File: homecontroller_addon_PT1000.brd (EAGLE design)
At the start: 60 x 100 mm, 44 parts, among them U1 OPA2188AIDGKR, U2 OPA2188AIDGKR, U3 REF3025AIDBZTG4, U4 ADS1015IDGST, X1 S2L3.50/10/90G

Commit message: update routing
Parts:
- added C10: 1000pF, supply2:CAPC3216X88N
- added R26: 0 Ohms, Vishay_By_element14_Batch_1:RESC3216X71N
- moved C2 43.4 mm to (31.9, 52.1), turned to 0 degrees
- moved U3 38.8 mm to (31.9, 55.9), turned to 180 degrees
- moved C7 34.5 mm to (3.95, 90.2), turned to 90 degrees
- moved C3 34.5 mm to (31.9, 59.7), turned to 0 degrees
- moved U4 24.8 mm to (8.35, 78.8), turned to 90 degrees
- moved R8 23.2 mm to (29.1, 77.0)
- moved R21 22.9 mm to (28.9, 92.8)
- moved R15 22.9 mm to (28.9, 85.1)
- moved R3 22.5 mm to (28.8, 65.0)
- moved R5 18.0 mm to (29.0, 68.9), turned to 180 degrees
- moved R11 17.6 mm to (29.0, 73.0), turned to 180 degrees
- moved R18 17.5 mm to (29.0, 81.1), turned to 180 degrees
- moved R24 17.5 mm to (29.0, 89.0), turned to 180 degrees
- moved R14 16.7 mm to (22.9, 82.9)
- moved R20 16.6 mm to (22.9, 90.9)
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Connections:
- net N$5 renamed -IN_0
- removed net +IN_1: R12.2, U1.5
- removed net +IN_2: R19.2, U2.3
- removed net +IN_3: R25.2, U2.5
- removed net N$1: R6.2, U1.3
- new net PE: C10.1, RV1.1, RV2.1, RV3.1, RV4.1
- new net SGND: C1.1, C4.1, C8.1, C9.1, R26.2
- net AGND: now also C10.2, R26.1, X1.2, X1.4, X1.6, X1.8; no longer C1.1, C4.1, C8.1, C9.1, RV1.1, RV2.1, RV3.1, RV4.1, X1.1, X1.3, X1.5, X1.7
- net PT1000_0: now also R6.2, U1.3, X1.1; no longer X1.2
- net PT1000_1: now also R12.2, U1.5, X1.3; no longer X1.4
- net PT1000_2: now also R19.2, U2.3, X1.5; no longer X1.6
- net PT1000_3: now also R25.2, U2.5, X1.7; no longer X1.8
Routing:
- net PT1000_3: track 0.00 -> 65.3 mm, vias 0 -> 3
- net PT1000_2: track 0.00 -> 60.4 mm, vias 0 -> 2
- net REF2.0V: track 0.00 -> 55.3 mm, vias 0 -> 5
- net -IN_3: track 0.00 -> 35.5 mm, vias 0 -> 4
- net PT1000_0: track 0.00 -> 31.1 mm, vias 0 -> 1
- net PT1000_1: track 0.00 -> 26.7 mm, vias 0 -> 1
- net AIN3: track 0.00 -> 17.4 mm, vias 0 -> 2
- net AIN2: track 0.00 -> 12.8 mm, vias 0 -> 2
- net -IN_2: track 0.00 -> 8.50 mm, vias 0 -> 2
- net AGND: track 0.00 -> 7.85 mm
- net N$4: track 0.00 -> 5.23 mm
- net VDD5V_F: track 0.00 -> 2.99 mm
- net N$1: track 0.00 -> 1.24 mm
- net N$7: track 0.00 -> 0.74 mm
- added copper zone on layer 1, net SGND
- added copper zone on layer 2, net SGND

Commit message: adopted wire plan
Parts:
- moved U4 2.54 mm to (10.9, 79.0), turned to 180 degrees
- moved U1 0.73 mm to (8.88, 71.1)
- moved R6 0.27 mm to (16.6, 66.9), turned to 180 degrees
- moved R12 0.23 mm to (16.5, 74.9), turned to 180 degrees
- moved R24 0.22 mm to (28.8, 88.9)
- moved R25 0.20 mm to (16.3, 91.0)
- moved R15 0.20 mm to (28.8, 85.1)
- moved R18 0.10 mm to (28.9, 81.1)
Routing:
- net -IN_1: track 0.00 -> 35.5 mm, vias 0 -> 4
- net -IN_2: track 8.50 -> 37.7 mm, vias 2 -> 4
- net PT1000_1: track 26.7 -> 10.2 mm, vias 1 -> 0
- net PT1000_2: track 60.4 -> 67.3 mm
- net AIN2: track 12.8 -> 19.2 mm
- net AGND: track 7.85 -> 14.0 mm, vias 0 -> 4
- net N$3: track 0.00 -> 4.94 mm
- net N$2: track 0.00 -> 4.58 mm
- net VDD5V_F: track 2.99 -> 6.45 mm
- net PT1000_3: track 65.3 -> 68.1 mm, vias 3 -> 2

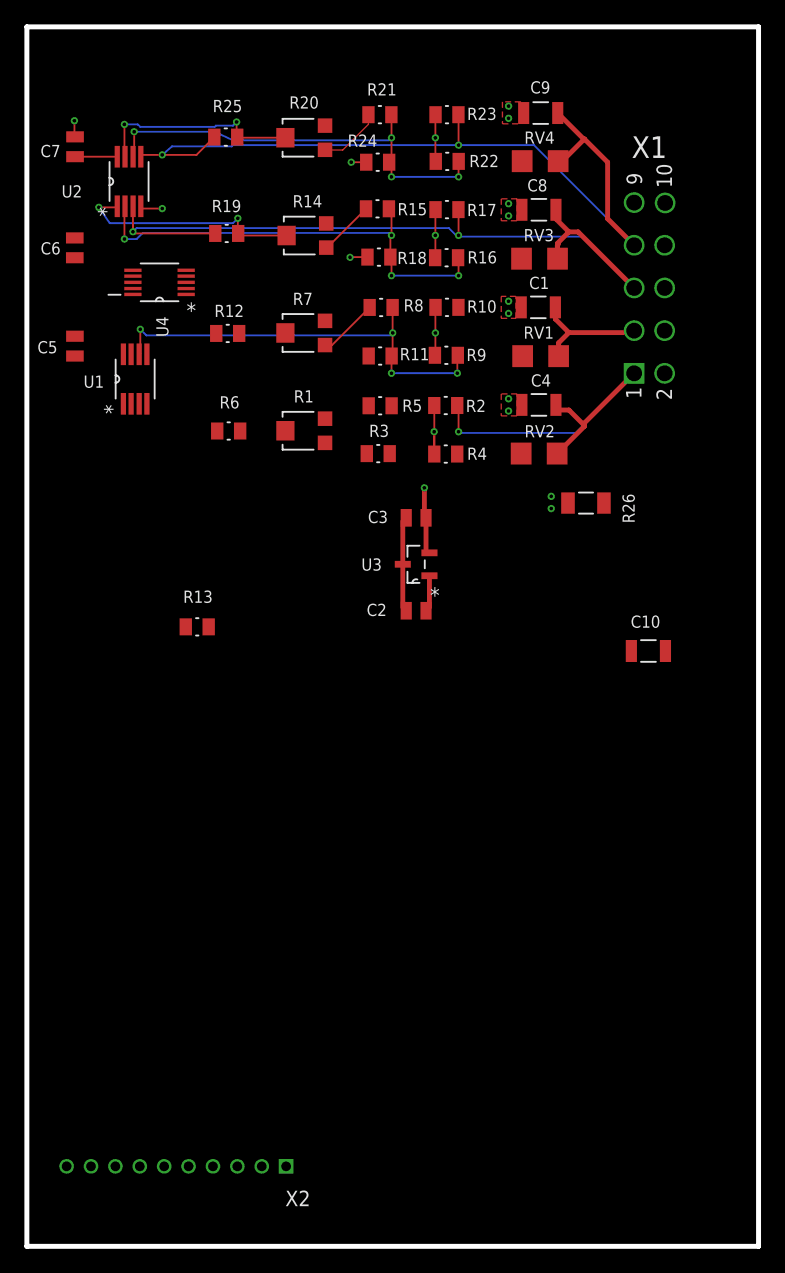
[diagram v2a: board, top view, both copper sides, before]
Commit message: change position of I2C ADC
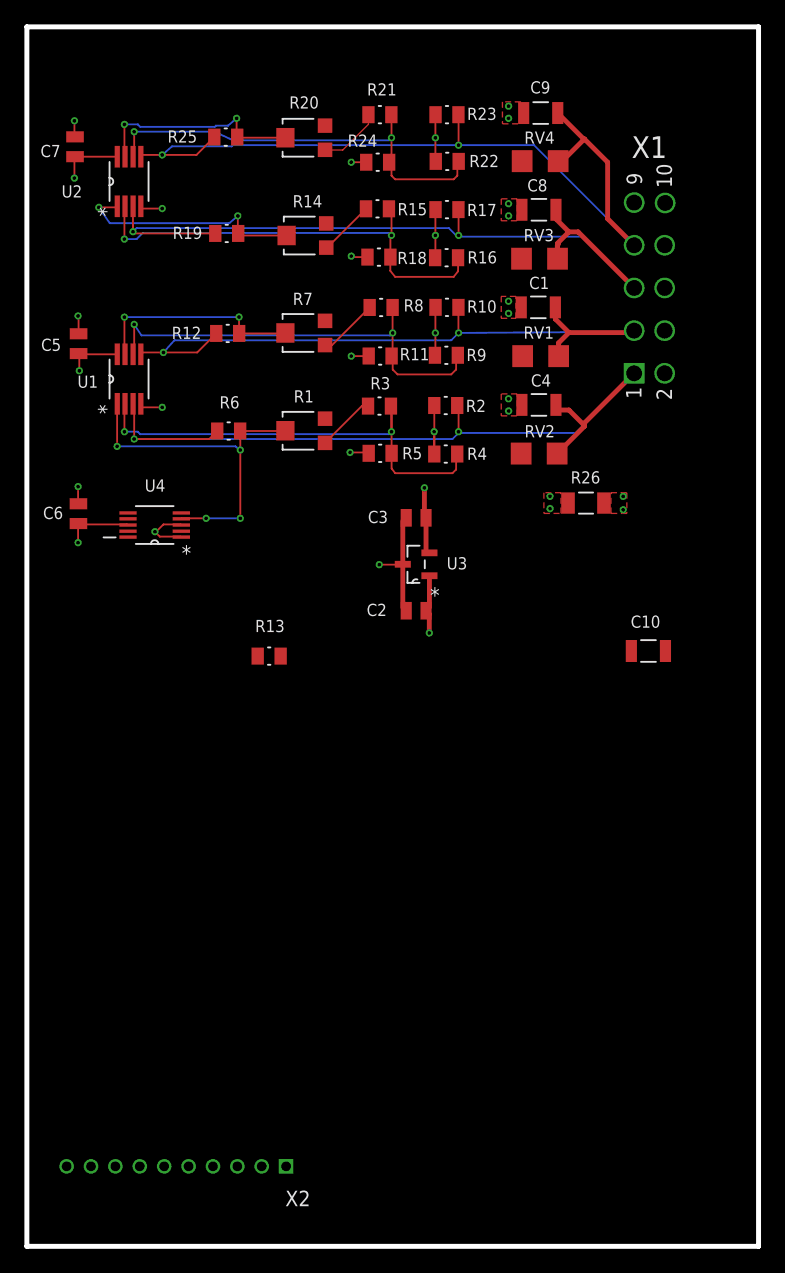
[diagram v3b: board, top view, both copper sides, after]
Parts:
- moved C6 21.8 mm to (4.23, 60.1)
- moved U4 19.9 mm to (10.5, 59.1)
- moved R13 6.37 mm to (19.9, 48.4)
- moved R3 3.90 mm to (28.9, 68.9)
- moved R5 3.90 mm to (29.0, 65.0)
- moved U1 0.50 mm to (8.38, 71.1)
- moved C5 0.36 mm to (4.24, 74.0)
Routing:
- net VDD5V_F: track 6.45 -> 145.6 mm, vias 0 -> 4
- net PT1000_1: track 10.2 -> 58.5 mm, vias 0 -> 2
- net -IN_0: track 0.00 -> 38.5 mm, vias 0 -> 2
- net PT1000_0: track 31.1 -> 68.2 mm, vias 1 -> 2
- net AIN0: track 0.00 -> 29.4 mm, vias 0 -> 4
- net AIN1: track 0.00 -> 17.6 mm, vias 0 -> 2
- net AGND: track 14.0 -> 29.2 mm, vias 4 -> 13
- net N$6: track 0.00 -> 4.77 mm
- net -IN_1: track 35.5 -> 36.3 mm, vias 4 -> 2
- net -IN_3: track 35.7 -> 36.1 mm, vias 4 -> 2
- net -IN_2: track 37.7 -> 37.5 mm, vias 4 -> 2
- added copper zone on layer 1, net AGND

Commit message: production status
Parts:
- added U$1, U$2: (no value), marks:PASSER_SMD4
- U4: device strasys_standard:SOP50P490X110-10N -> ADS1015:SOP50P490X110-10N
- moved R26 9.50 mm to (46.0, 51.5)
- moved R13 9.31 mm to (16.0, 56.9), turned to 90 degrees
- moved C10 6.38 mm to (54.1, 43.3), turned to 180 degrees
- moved X2 1.17 mm to (21.1, 5.40)
- moved C7 0.20 mm to (4.15, 90.2)
- moved U4 0.09 mm to (10.4, 59.2)
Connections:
- net +3.3V: now also X2.P$10; no longer X2.P$1
- net AGND: now also X2.P$1; no longer X2.P$10
- net I2C1_SCL: now also X2.P$3; no longer X2.P$8
- net I2C1_SDA: now also X2.P$4; no longer X2.P$7
- net P9_14: now also X2.P$7; no longer X2.P$4
- net P9_15: now also X2.P$8; no longer X2.P$3
- net P9_16: now also X2.P$9; no longer X2.P$2
- net UART2_RXD: now also X2.P$6; no longer X2.P$5
- net UART2_TXD: now also X2.P$5; no longer X2.P$6
- net VDD5V_F: now also X2.P$2; no longer X2.P$9
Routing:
- net +3.3V: track 0.00 -> 67.8 mm, vias 0 -> 4
- net P9_14: track 0.00 -> 66.3 mm, vias 0 -> 2
- net I2C1_SDA: track 0.00 -> 60.9 mm
- net I2C1_SCL: track 0.00 -> 57.2 mm
- net AIN3: track 17.8 -> 51.8 mm, vias 2 -> 4
- net AIN2: track 19.5 -> 44.0 mm, vias 2 -> 3
- net AIN1: track 17.6 -> 37.6 mm, vias 2 -> 4
- net VDD5V_F: track 145.6 -> 157.2 mm
- net PT1000_1: track 58.5 -> 62.8 mm
- net PT1000_0: track 68.2 -> 70.4 mm
- net N$1: track 1.24 -> 0.00 mm
- net PT1000_2: track 67.3 -> 68.4 mm
- net N$7: track 0.74 -> 0.00 mm
- net PT1000_3: track 68.1 -> 68.6 mm
- net AGND: track 29.2 -> 28.7 mm, vias 13 -> 15
- added copper zone on layer 1, net PE
- added copper zone on layer 16, net PE
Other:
- board text added: "EL-100-010-02"
- board text added: "Rev. 1.0 - proto"
- board text added: "bottom"
- board text added: "top"
- board text added: "www.strasys.at"

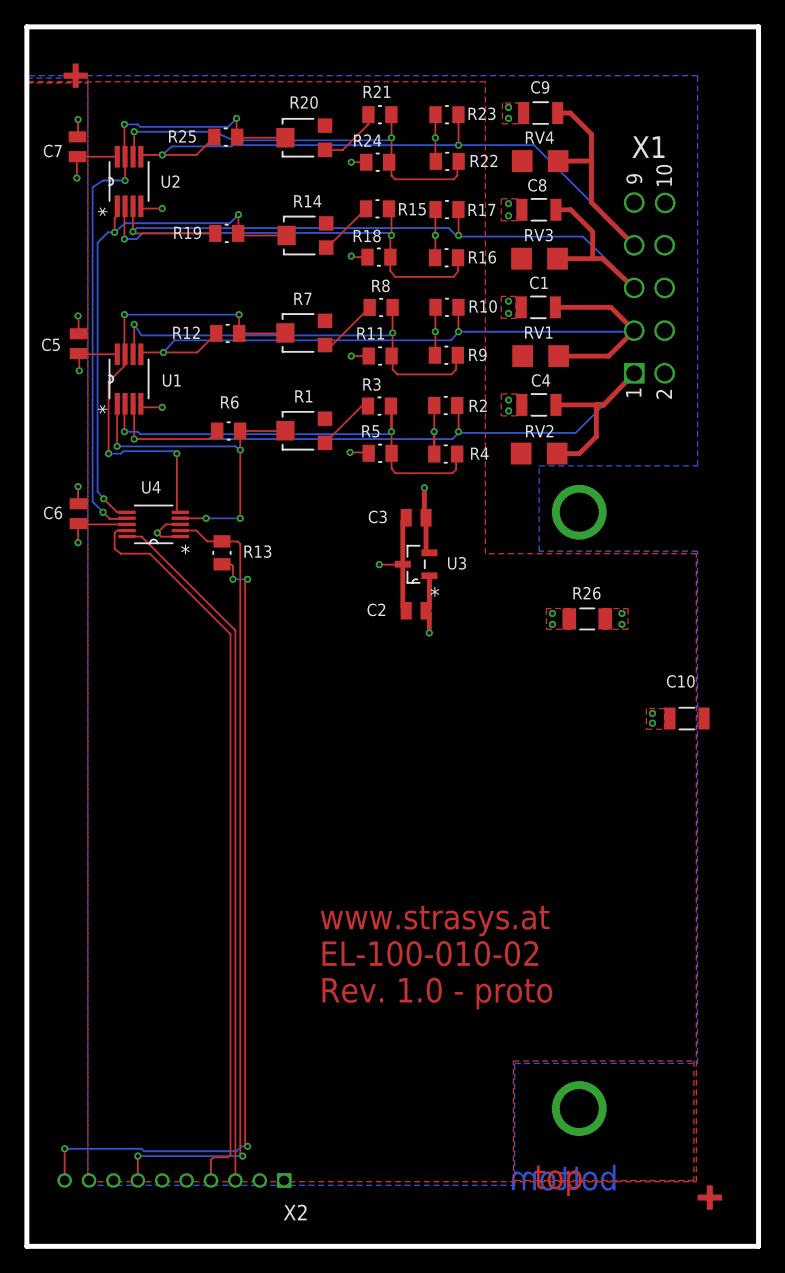
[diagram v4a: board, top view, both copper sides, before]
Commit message: PCB - production status
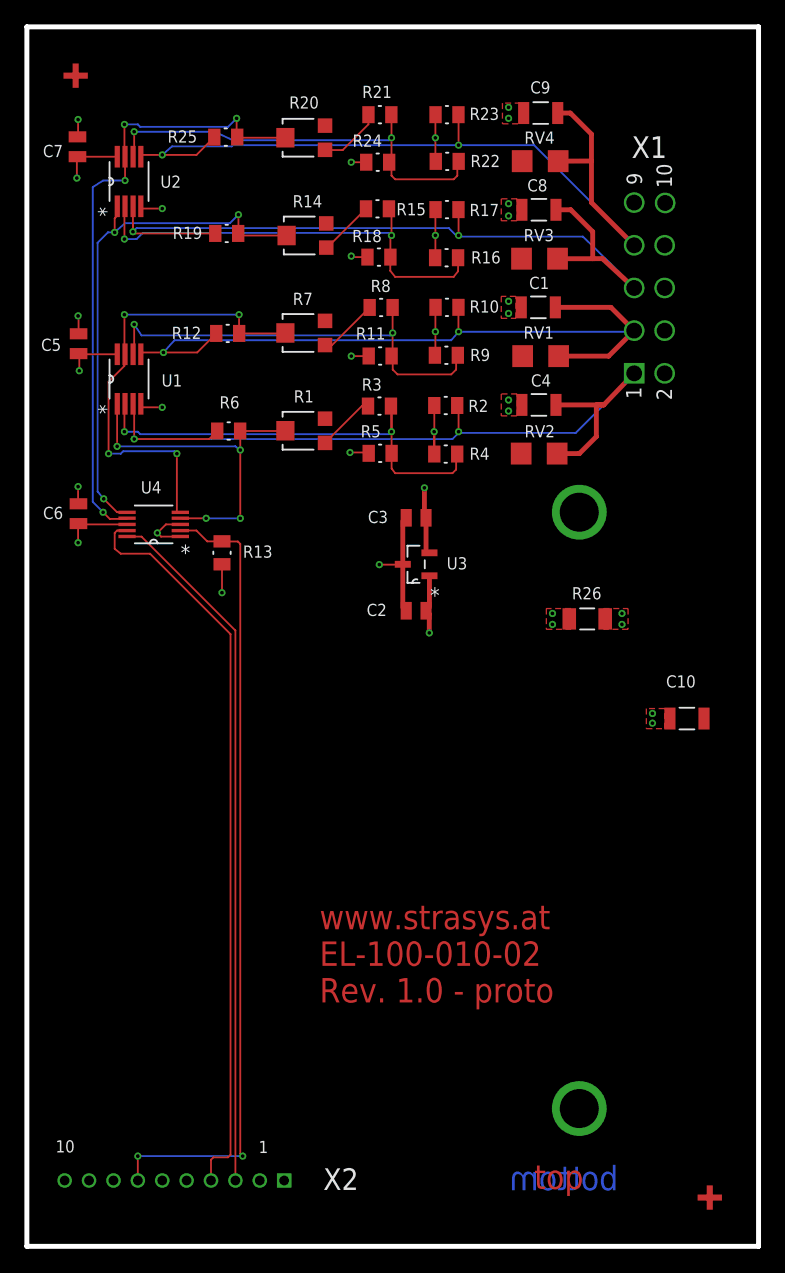
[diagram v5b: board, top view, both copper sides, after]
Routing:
- net +3.3V: track 67.8 -> 102.5 mm, vias 4 -> 1
- net REF2.0V: track 55.3 -> 58.3 mm
- net VDD5V_F: track 157.2 -> 158.0 mm
- added copper zone on layer 15, net N$8
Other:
- board text added: "1"
- board text added: "10"

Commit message: components price opti
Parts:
- R11, R18, R24, R5: value 1K Ohm -> 1K Ohms

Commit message: optimisation of BOM
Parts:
- C2, C3, C5, C6, C7: value 0.1uF -> 100nF; device Kemet_By_element14_1:CAPC2013X88N -> Kemet_By_element14_1:CAPC2013X110N
- R16, R22, R4, R9: value 32.4K Ohms -> 32.4kohms

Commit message: update
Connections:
- new net REF2.5V: C3.2, R2.1, R4.2, U3.2
- net REF2.0V: no longer C3.2, R2.1, R4.2, U3.2
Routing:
- net REF2.0V: track 58.3 -> 49.4 mm
- net REF2.5V: track 0.00 -> 6.97 mm
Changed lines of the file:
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@@
 </signal>
 <signal name="REF2.0V">
-<contactref element="U3" pad="2"/>
-<contactref element="R2" pad="1"/>
-<contactref element="R4" pad="2"/>
-<contactref element="C3" pad="2"/>
 <contactref element="R9" pad="2"/>
 <contactref element="R10" pad="1"/>
@@
 <wire x1="33.5" y1="82.9" x2="31.9" y2="82.9" width="1" layer="15"/>
 <via x="33.4" y="66.8" extent="1-16" drill="0.3"/>
-<wire x1="33.4102" y1="64.97" x2="33.4102" y2="68.95" width="0.15" layer="1"/>
-<wire x1="32.7328" y1="59.74" x2="32.7328" y2="57.1492" width="0.4" layer="1"/>
-<wire x1="32.7328" y1="57.1492" x2="33.0122" y2="56.8698" width="0.15" layer="1"/>
 <via x="32.6" y="62.2" extent="1-16" drill="0.3"/>
 <wire x1="32.6" y1="62.2" x2="32.6" y2="59.8728" width="0.4" layer="1"/>
-<wire x1="32.6" y1="59.8728" x2="32.7328" y2="59.74" width="0.15" layer="1"/>
-<wire x1="33.4102" y1="64.97" x2="33.4102" y2="66.7898" width="0.15" layer="1"/>
 <wire x1="33.4102" y1="66.7898" x2="33.4" y2="66.8" width="0.15" layer="1"/>
 <wire x1="33.4" y1="66.8" x2="31.9" y2="66.8" width="1" layer="15"/>
@@
 </polygon>
 </signal>
+<signal name="REF2.5V">
+<contactref element="U3" pad="2"/>
+<contactref element="R2" pad="1"/>
+<contactref element="R4" pad="2"/>
+<contactref element="C3" pad="2"/>
+<wire x1="33.4102" y1="64.97" x2="33.4102" y2="68.95" width="0.15" layer="1"/>
+<wire x1="32.7328" y1="59.74" x2="32.7328" y2="57.1492" width="0.4" layer="1"/>
+<wire x1="32.7328" y1="57.1492" x2="33.0122" y2="56.8698" width="0.15" layer="1"/>
+<wire x1="32.7328" y1="59.74" x2="33.4102" y2="64.97" width="0" layer="19" extent="1-1"/>
+</signal>
 </signals>
